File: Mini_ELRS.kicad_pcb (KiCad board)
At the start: 4 copper layers, 26.7 x 15.8 mm, 30 parts, among them J1 Conn_01x02, J2 Conn_01x03_MountingPin, J3 Conn_01x04, J4 Conn_01x03_MountingPin, J5 Conn_01x03_MountingPin, J6 Conn_01x03_MountingPin, Q1 Q_NMOS_GSD, Q2 Q_NMOS_GSD, U1 ESP32-PICO-D4, U2 TC2014-3.3VxCTTR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

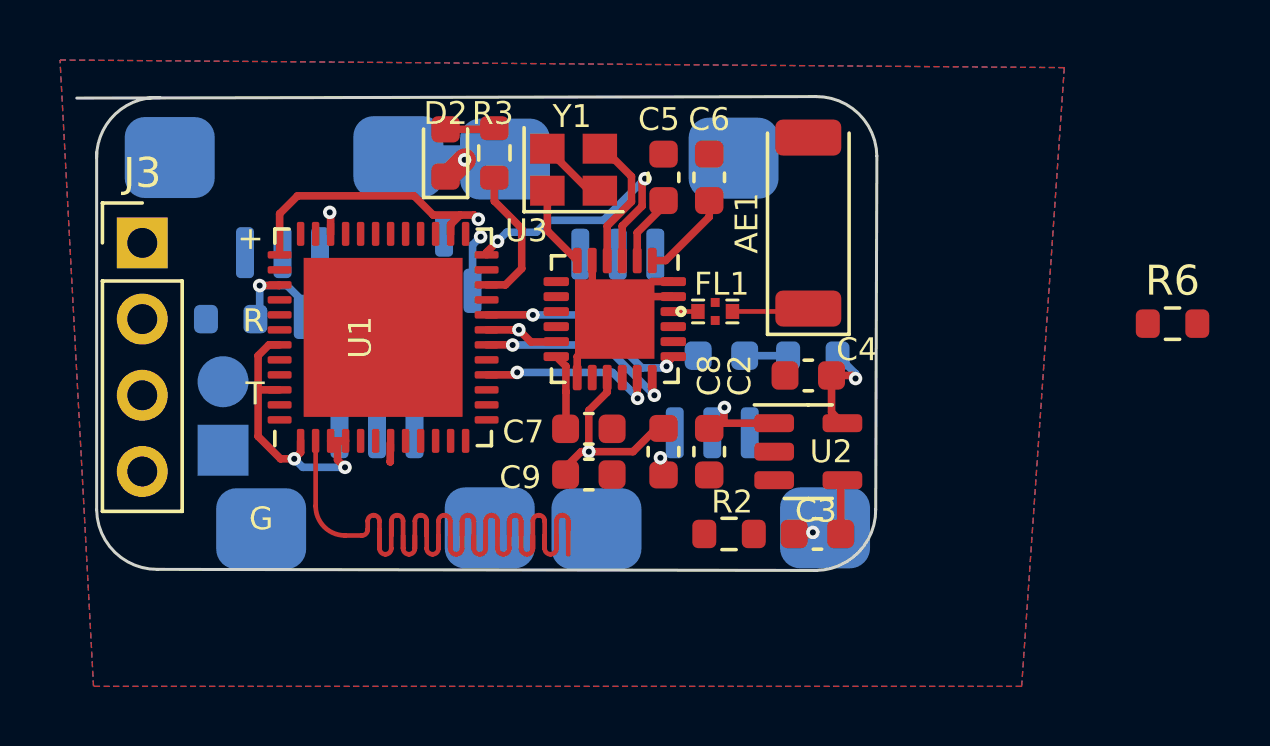
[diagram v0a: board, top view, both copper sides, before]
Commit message: finished pcb. using normal layer stack
Signed-off-by: huangzzk <huangcmzzk@gmail.com>
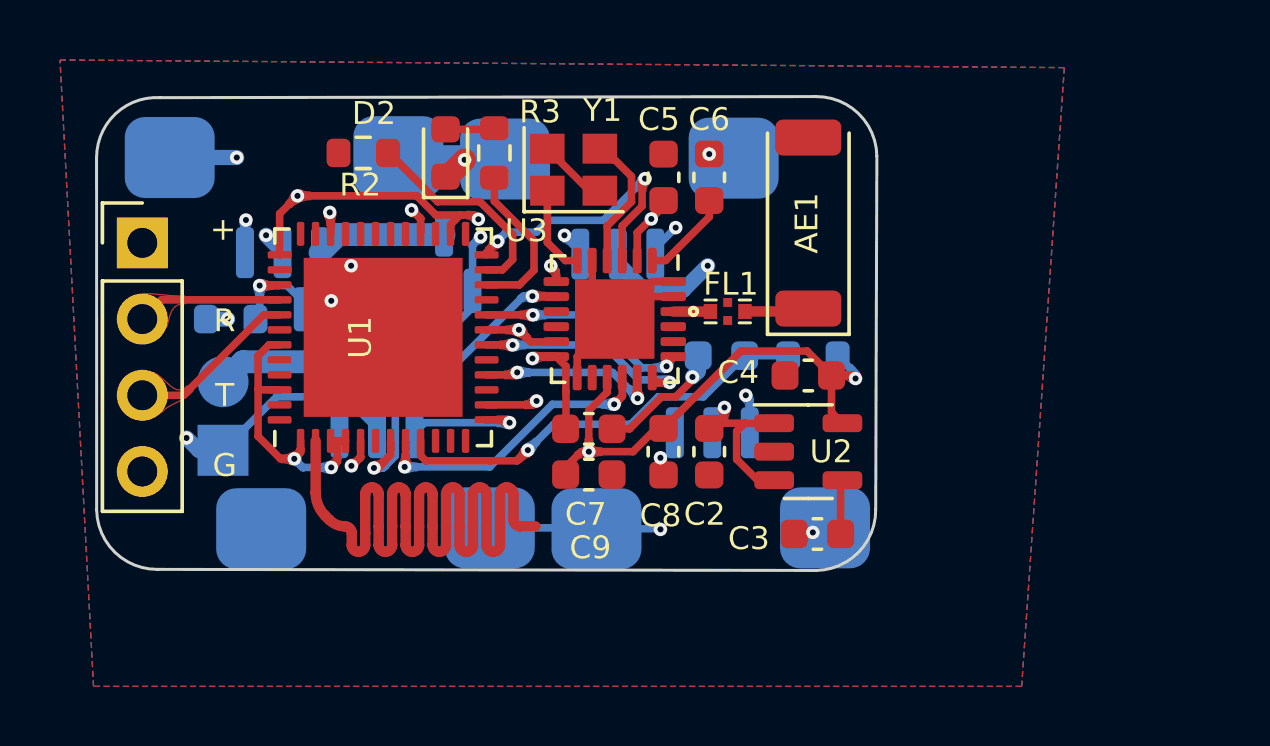
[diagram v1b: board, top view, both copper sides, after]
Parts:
- removed R6: 10K, Resistor_SMD:R_0603_1608Metric
- moved R2 17.6 mm to (107.3, 57.6), turned to 180 degrees
- moved R5 1.17 mm to (109.2, 63.7)
- moved FL1 0.42 mm to (119.5, 62.9)
- moved Q1 0.25 mm to (106.3, 63.8)
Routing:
- net +3V3: track 42.9 -> 60.9 mm, vias 6 -> 7
- net GND: track 13.6 -> 31.5 mm, vias 3 -> 11
- net +BATT: track 2.52 -> 18.0 mm, vias 1 -> 4
- net Net-(C1-Pad1): track 1.45 -> 14.3 mm, vias 0 -> 1
- net /PWM2: track 0.00 -> 12.3 mm, vias 0 -> 2
- net /BUSY: track 0.00 -> 12.2 mm, vias 0 -> 2
- net /DIO1: track 0.62 -> 10.7 mm, vias 0 -> 2
- net /MISO: track 0.00 -> 9.73 mm, vias 0 -> 2
- net Net-(C5-Pad1): track 4.70 -> 12.4 mm, vias 0 -> 2
- net /PWM3: track 8.01 -> 15.6 mm, vias 2 -> 3
- net /PWM1: track 0.00 -> 7.38 mm, vias 0 -> 2
- net Net-(R2-Pad1): track 0.00 -> 7.14 mm
- net /TX: track 0.00 -> 5.69 mm
- net /ESP32_ANT: track 38.4 -> 32.8 mm
- net /RX: track 0.00 -> 4.84 mm
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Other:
- board size 26.7 x 15.8 mm -> 26 x 15.8 mm
